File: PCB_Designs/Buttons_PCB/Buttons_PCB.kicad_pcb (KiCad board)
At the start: 2 copper layers, 50 x 158.8 mm, 84 parts, among them P1 CONN_02X05, P2 CONN_01X01, P3 CONN_01X01, P4 CONN_01X01, P5 CONN_01X01, U1 CHERRY-MX, U10 CHERRY-MX, U11 CHERRY-MX, U12 CHERRY-MX, U13 MCP23017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

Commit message: Nya Photomasks Buttons
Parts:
- moved R25 152.2 mm to (217.1, 66.3), turned to 270 degrees
- moved C1 149.5 mm to (217.1, 70.3), turned to 270 degrees
- moved D1 139.5 mm to (208.9, 70.0), turned to 270 degrees
- moved U1 139.5 mm to (208.9, 70.0), turned to 270 degrees
- moved R1 138.6 mm to (212.8, 78.8), turned to 180 degrees
- moved P4 137.9 mm to (214.1, 82.8), turned to 270 degrees
- moved R13 135.8 mm to (215.1, 89.8), turned to 90 degrees
- moved R14 132.4 mm to (212.5, 89.8), turned to 90 degrees
- moved R26 129.6 mm to (198.1, 66.3), turned to 270 degrees
- moved R15 129.0 mm to (210.0, 89.8), turned to 90 degrees
- moved R20 128.4 mm to (213.8, 106.7), turned to 270 degrees
- moved C2 126.4 mm to (198.1, 70.3), turned to 270 degrees
- moved R16 125.6 mm to (207.5, 89.9), turned to 90 degrees
- moved R19 124.8 mm to (211.3, 106.7), turned to 270 degrees
- moved R18 121.3 mm to (208.7, 106.7), turned to 270 degrees
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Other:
- board size 50 x 158.8 mm -> 158.8 x 50 mm

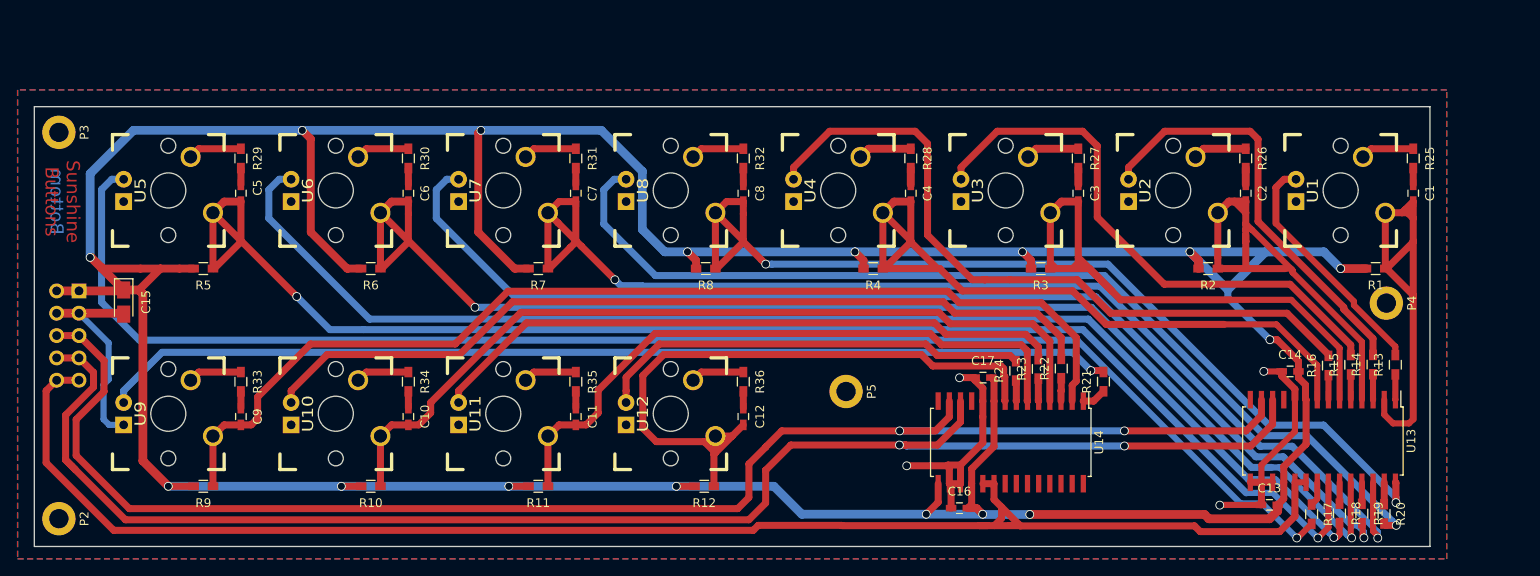
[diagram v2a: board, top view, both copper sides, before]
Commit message: Edited Buttons and sliders for manufacturability
* All vias updated to 1.5 or 2 mm diameter
* Slight designchanges to get rid of drills close to edges in Buttons
* New Photomasks printed for Buttons and Sliders
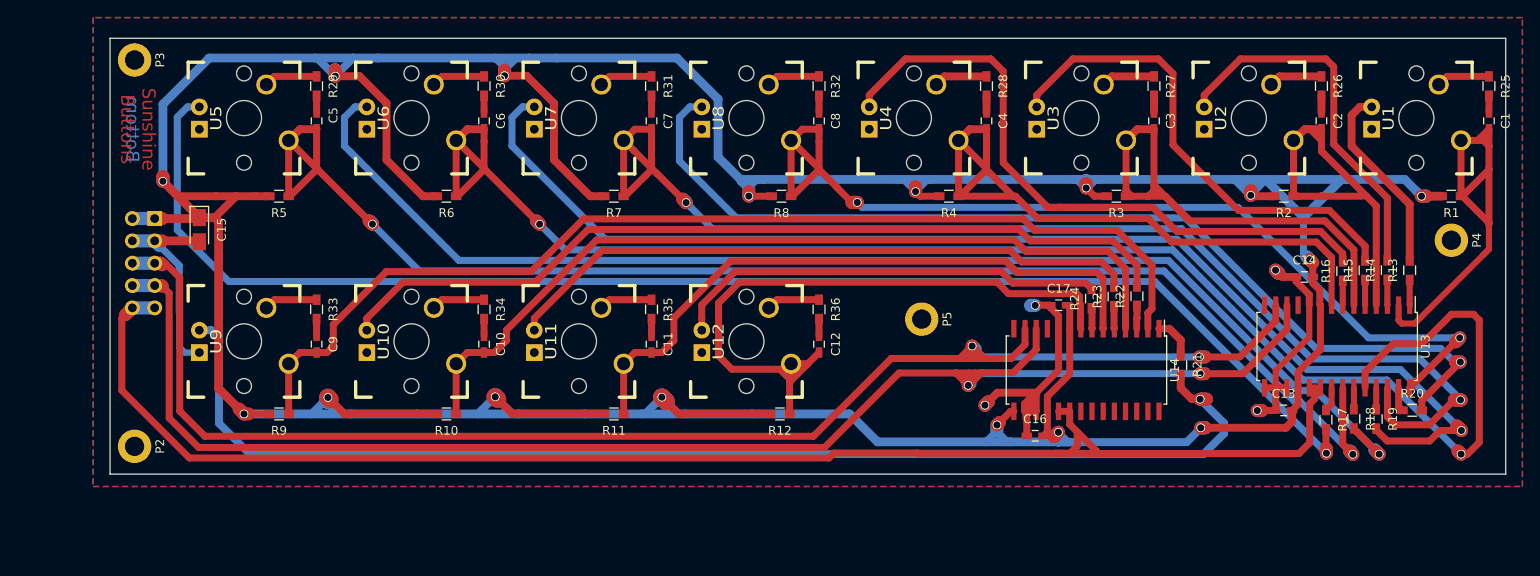
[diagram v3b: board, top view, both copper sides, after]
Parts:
- moved R20 12.2 mm to (217.0, 95.0), turned to 0 degrees
- moved C12 11.9 mm to (149.5, 87.4)
- moved C16 11.9 mm to (174.1, 97.9)
- moved C8 11.9 mm to (149.5, 62.0)
- moved D12 11.9 mm to (141.3, 87.1)
- moved P5 11.9 mm to (161.2, 84.6)
- moved R12 11.9 mm to (145.1, 95.4)
- moved R2 11.9 mm to (202.4, 70.6)
- moved R24 11.9 mm to (180.5, 82.3)
- moved R36 11.9 mm to (149.5, 83.5)
- moved R4 11.9 mm to (164.3, 70.6)
- moved U12 11.9 mm to (141.3, 87.1)
- moved C2 11.9 mm to (206.7, 62.0)
- moved D2 11.9 mm to (198.4, 61.7)
- moved D3 11.9 mm to (179.4, 61.7)
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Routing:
- net /VDD: track 471.7 -> 570.2 mm
- net Net-(C6-Pad2): track 151.2 -> 184.5 mm
- net Net-(D9-Pad1): track 115.5 -> 139.9 mm
- net Net-(C2-Pad2): track 57.9 -> 46.3 mm
- net Net-(D7-Pad1): track 129.0 -> 139.3 mm
- net Net-(C3-Pad2): track 67.2 -> 59.4 mm
- net Net-(D3-Pad1): track 63.4 -> 55.6 mm
- net Net-(D4-Pad1): track 80.9 -> 73.3 mm
- net Net-(C4-Pad2): track 85.7 -> 78.6 mm
- net Net-(D1-Pad1): track 27.4 -> 22.0 mm
- net Net-(D2-Pad1): track 48.1 -> 42.7 mm
- net Net-(D5-Pad1): track 165.2 -> 160.8 mm
- net /GND: track 101.2 -> 105.5 mm
- net Net-(C7-Pad2): track 138.3 -> 142.6 mm
- net /S_CLK_L: track 177.8 -> 173.6 mm
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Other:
- board size 158.8 x 50 mm -> 158.8 x 49.6 mm

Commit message: Manufacture files added
* Gerbers created
* Drillfiles created
* G-CODE generated (milling information)
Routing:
- net Net-(C3-Pad2): track 59.4 -> 65.8 mm
- net /INT: track 171.5 -> 170.0 mm

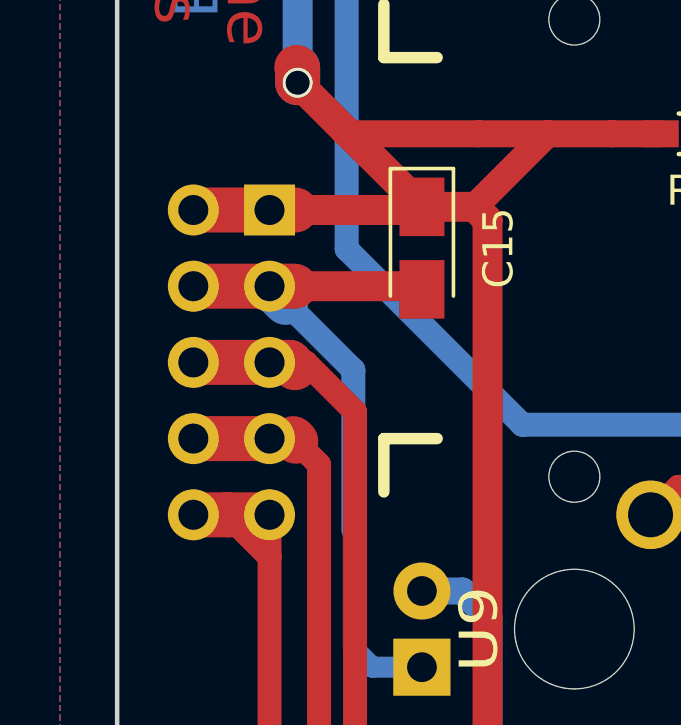
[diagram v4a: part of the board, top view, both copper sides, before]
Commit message: Hotfixes, updates and Photomask
* Edited small error in component placing (OLED_LCD)
* Updated all photomasks in light of recent events
* Generated photomask for OLED_LCD (.pdf)
* Updated all Gerberfiles (.gbr)
* Updated all drillfiles, now merging "plated" and unplated TH (.drl)
* With merge; all Non Plated Through Hole drills deleted (-NPTH.drl)
* Generated new G-CODE for all PCB (.ngc, .svg)
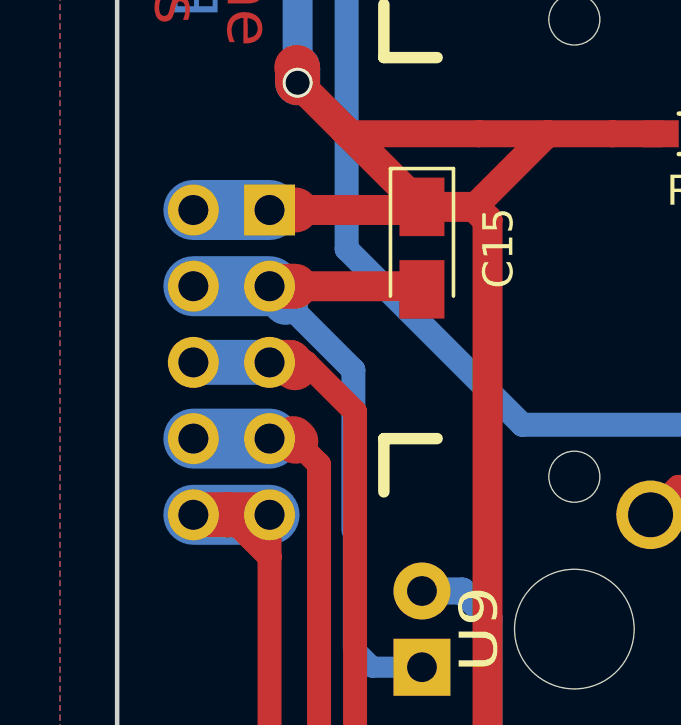
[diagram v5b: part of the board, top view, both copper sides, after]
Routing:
- net /INT: track 170.0 -> 172.6 mm
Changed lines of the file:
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@@
     (thickness 1.6)
     (drawings 6)
-    (tracks 861)
+    (tracks 862)
     (zones 0)
     (modules 84)
@@
   )
   (setup
-    (last_trace_width 0.7)
+    (last_trace_width 2)
     (user_trace_width 0.7)
     (user_trace_width 0.8)
@@
   (gr_line (start 227.6342 52.65) (end 68.879962 52.65) (layer Edge.Cuts) (width 0.15))
   (gr_line (start 227.6342 102.2016) (end 227.6342 52.649998) (layer Edge.Cuts) (width 0.15))
-  (segment (start 71.4242 73.1516) (end 73.9642 73.1516) (width 1.5) (layer F.Cu) (net 1))
+  (segment (start 73.9642 73.1516) (end 71.4242 73.1516) (width 2) (layer B.Cu) (net 1))
   (segment (start 179.9226 69.68) (end 179.9226 68.802501) (width 1.5) (layer B.Cu) (net 1))
   (segment (start 218.06421 70.6116) (end 218.5384 70.6116) (width 1.5) (layer B.Cu) (net 1))
@@
   (segment (start 146.3542 89.6616) (end 148.2592 89.6616) (width 0.8) (layer F.Cu) (net 13))
   (segment (start 148.2592 89.6616) (end 149.5292 88.3916) (width 0.8) (layer F.Cu) (net 13))
-  (segment (start 71.4242 75.6916) (end 73.9642 75.6916) (width 1.5) (layer F.Cu) (net 14))
+  (segment (start 71.4242 75.6916) (end 73.9642 75.6916) (width 2) (layer B.Cu) (net 14))
   (segment (start 76.7582 83.8196) (end 76.7582 78.4856) (width 0.8) (layer B.Cu) (net 14))
   (segment (start 76.7582 78.4856) (end 74.504199 76.231599) (width 0.8) (layer B.Cu) (net 14))
@@
   (segment (start 149.5292 86.4916) (end 149.5292 84.5816) (width 0.8) (layer F.Cu) (net 14))
   (segment (start 225.7292 59.1816) (end 225.7292 61.0866) (width 0.8) (layer F.Cu) (net 14))
-  (segment (start 71.4242 80.7716) (end 73.9642 80.7716) (width 1.5) (layer F.Cu) (net 15))
+  (segment (start 71.4242 80.7716) (end 73.9642 80.7716) (width 2) (layer B.Cu) (net 15))
   (segment (start 165.1 90.721324) (end 158.629476 90.721324) (width 0.8) (layer F.Cu) (net 15))
   (segment (start 158.629476 90.721324) (end 150.1642 99.1866) (width 0.8) (layer F.Cu) (net 15))
@@
   (segment (start 202.7542 85.7916) (end 202.7542 83.0016) (width 0.8) (layer F.Cu) (net 15))
   (via (at 192.8742 90.7916) (size 1) (drill 0.8) (layers F.Cu B.Cu) (net 15))
-  (segment (start 71.4242 78.2316) (end 73.9642 78.2316) (width 1.5) (layer F.Cu) (net 16))
+  (segment (start 71.4242 78.2316) (end 73.9642 78.2316) (width 1.5) (layer B.Cu) (net 16))
   (segment (start 76.814212 79.879531) (end 75.166281 78.2316) (width 0.8) (layer F.Cu) (net 16))
   (segment (start 76.814212 95.051612) (end 76.814212 79.879531) (width 0.8) (layer F.Cu) (net 16))
@@
   (segment (start 149.5292 82.3816) (end 144.7442 82.3816) (width 0.8) (layer F.Cu) (net 52))
   (segment (start 144.7442 82.3816) (end 143.8142 83.3116) (width 0.8) (layer F.Cu) (net 52))
+  (segment (start 71.4242 83.3116) (end 73.9642 83.3116) (width 2) (layer B.Cu) (net 53))
   (segment (start 72.56 83.3116) (end 73.9642 83.3116) (width 1.5) (layer F.Cu) (net 53))
   (segment (start 71.4242 83.3116) (end 72.56 83.3116) (width 1.5) (layer F.Cu) (net 53))

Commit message: Added missing 10k R on OLED board, diodes on Buttons board
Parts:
- added D13: D_Schottky, Diodes_SMD:D_0603, F.Cu at (205.3, 96.6)
- added D14: D_Schottky, Diodes_SMD:D_0603, F.Cu at (178.7, 98.0)
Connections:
- U13 pad 19: /INT -> Net-(D13-Pad2)
- U13 pad 20: /INT -> Net-(D13-Pad2)
- U14 pad 19: /INT -> Net-(D14-Pad2)
- U14 pad 20: /INT -> Net-(D14-Pad2)
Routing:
- net /INT: track 172.6 -> 155.8 mm
- net Net-(D13-Pad2): track 0.00 -> 4.91 mm
- net Net-(D14-Pad2): track 0.00 -> 3.59 mm
